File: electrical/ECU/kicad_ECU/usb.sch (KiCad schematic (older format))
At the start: 23 parts

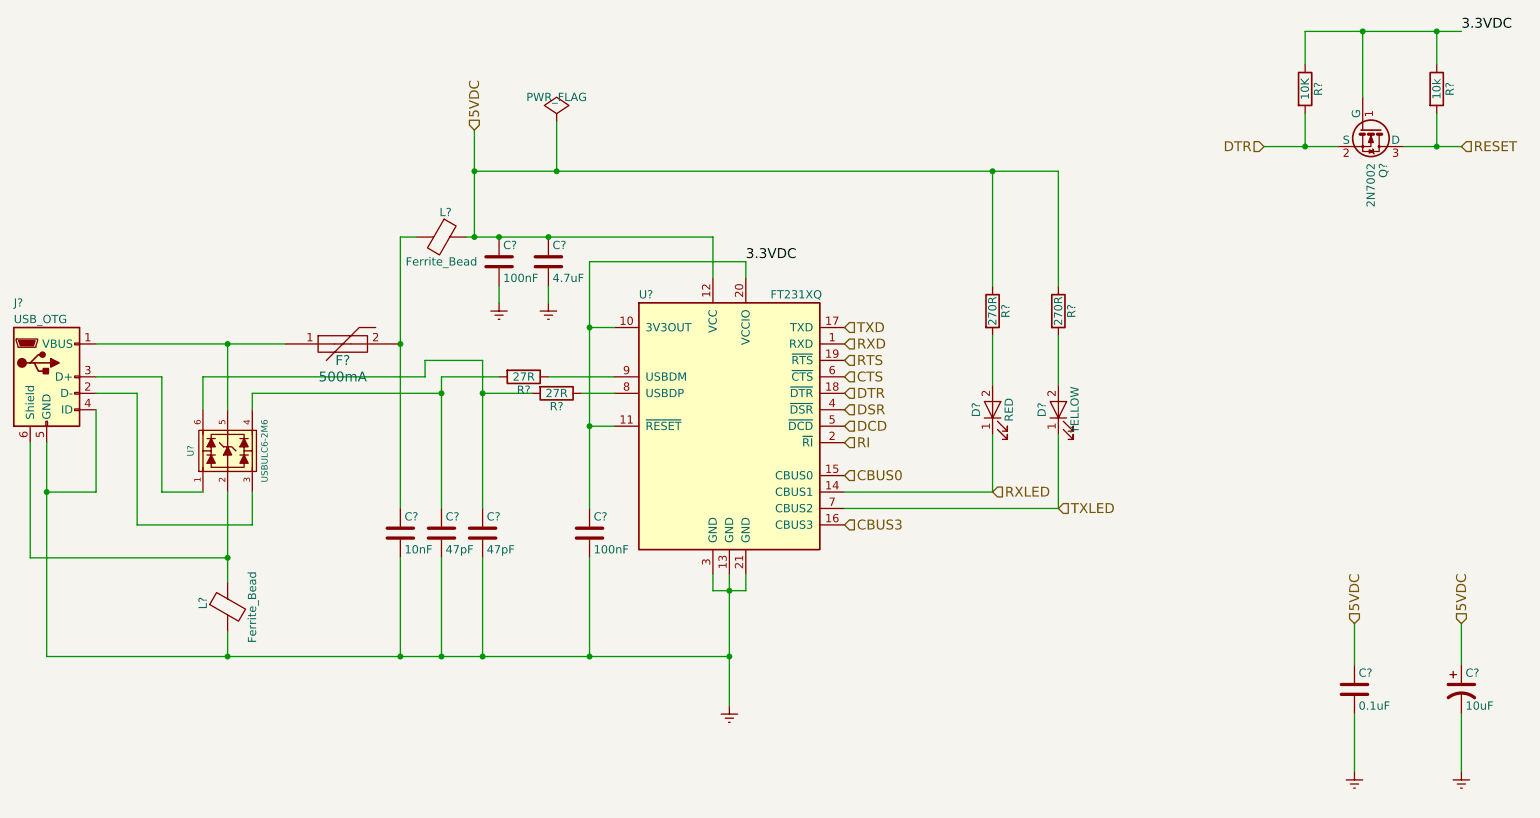
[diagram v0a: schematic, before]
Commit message: fixed some naming errors and initial round of double checking
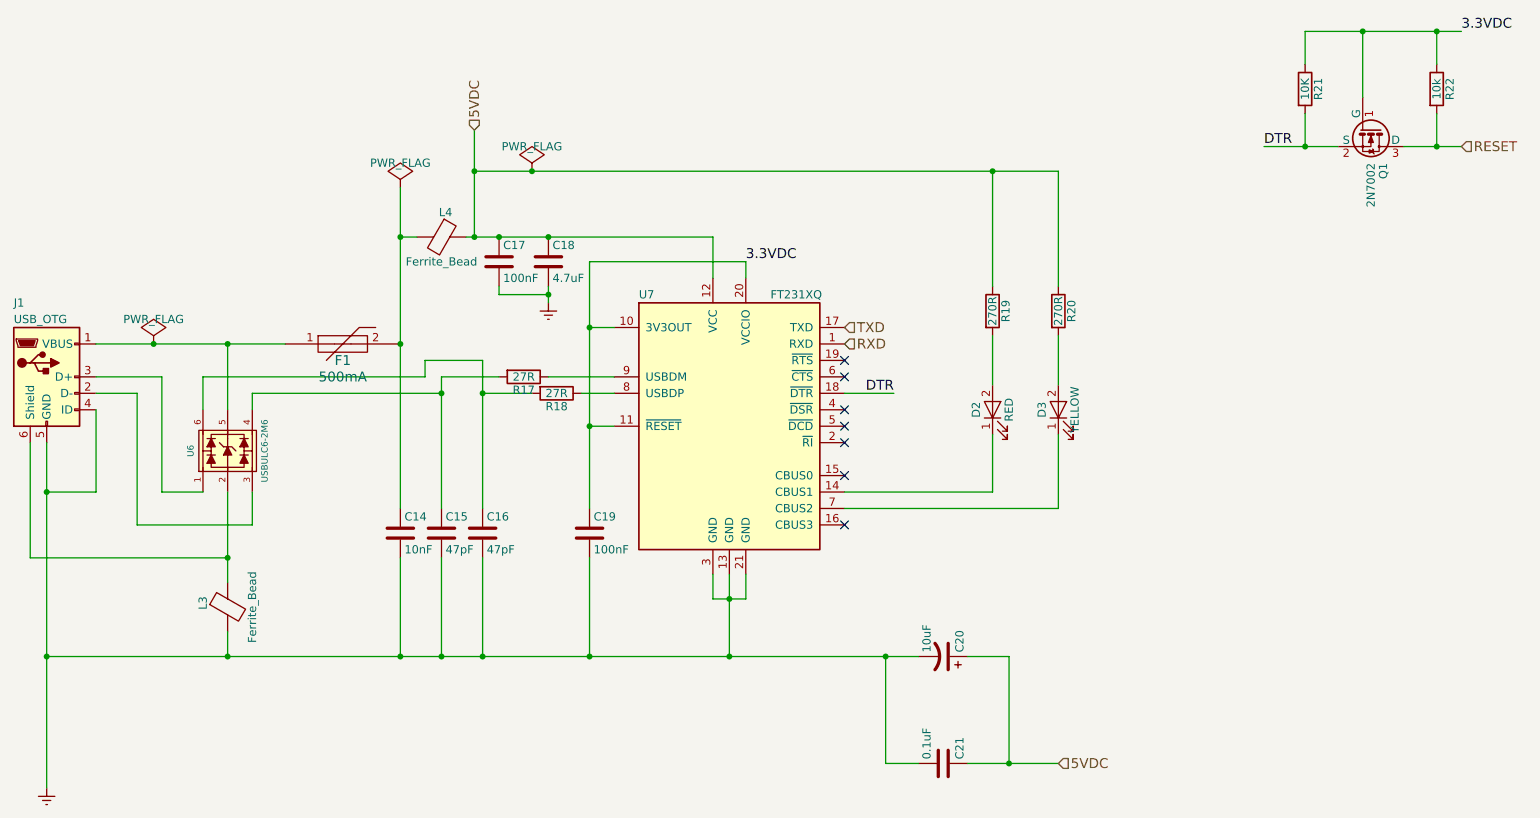
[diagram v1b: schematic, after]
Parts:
- gave numbers to parts that had none: 23
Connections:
- net CBUS0: no longer names the net of U7.15 (CBUS0)
- net CBUS3: no longer names the net of U7.16 (CBUS3)
- net CTS: no longer names the net of U7.6 (~CTS)
- net DCD: no longer names the net of U7.5 (~DCD)
- net DSR: no longer names the net of U7.4 (~DSR)
- net RI: no longer names the net of U7.2 (~RI)
- net RTS: no longer names the net of U7.19 (~RTS)
- net RXLED: no longer names the net of D2.1 (K), U7.14 (CBUS1)
- net TXLED: no longer names the net of D3.1 (K), U7.7 (CBUS2)
- no-connect marks 0 -> 7
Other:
- moved on the sheet: C20, C21
